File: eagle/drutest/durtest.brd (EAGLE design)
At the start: 100 x 80 mm, 2 parts, among them U1 XC3S400TQ144

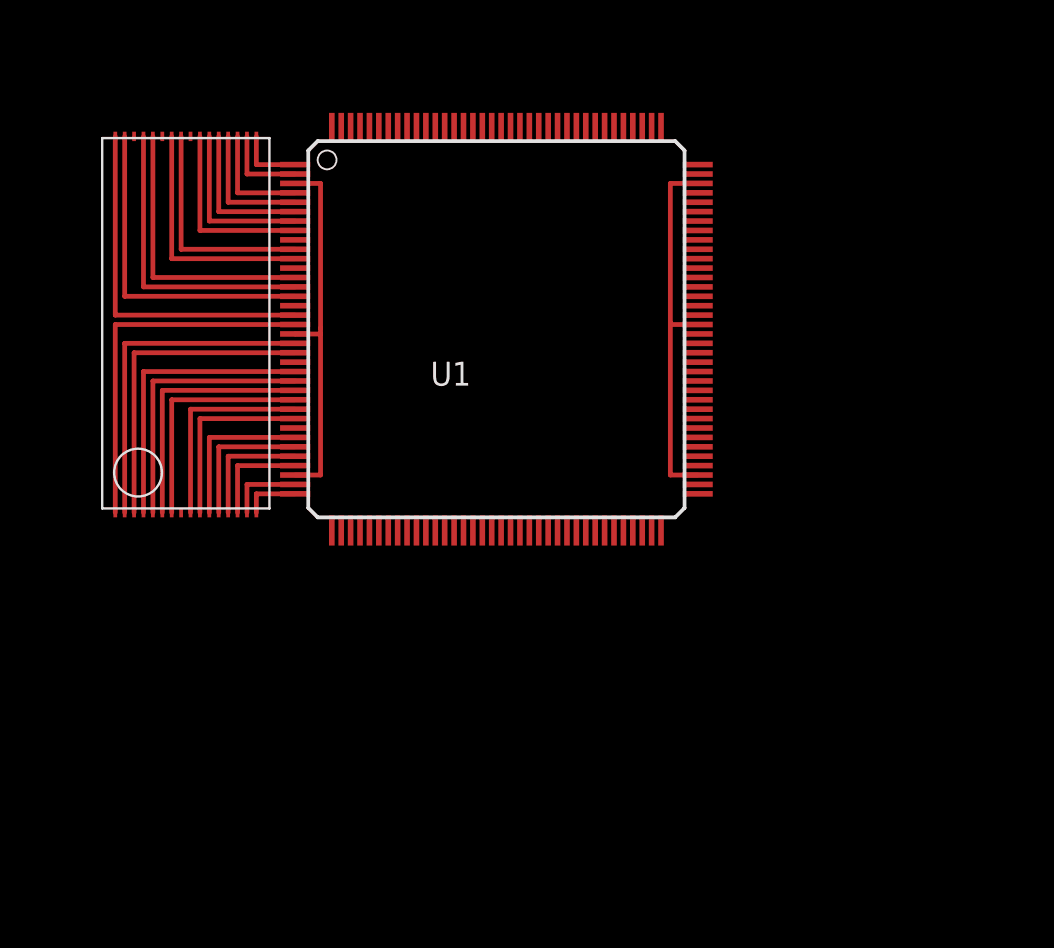
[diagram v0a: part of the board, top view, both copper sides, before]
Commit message: durtest is becoming the best board... but requires proper fabbing
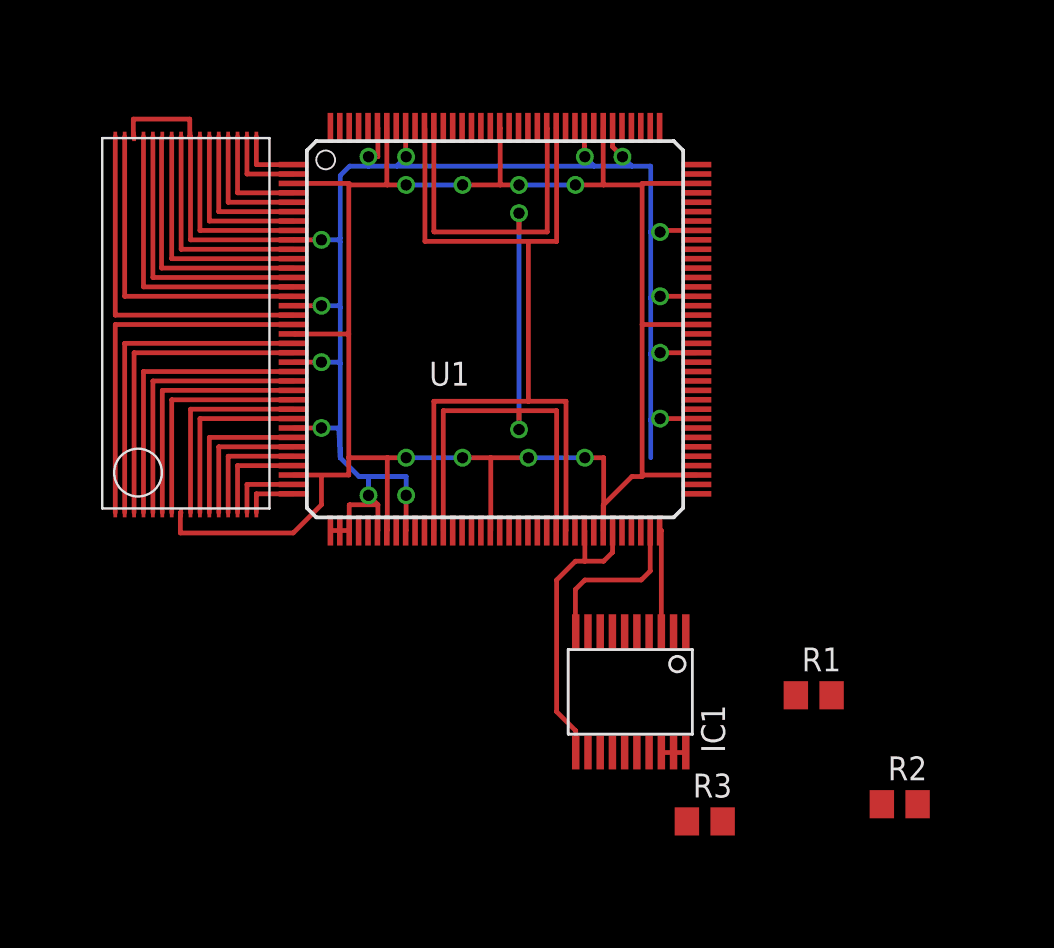
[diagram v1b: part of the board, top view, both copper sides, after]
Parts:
- added IC1: XCF02S, smd-special:VO20
- added R1, R2, R3: 100, rcl:R0805
- moved U1 0.07 mm to (50.7, 36.8)
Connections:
- removed net N$30: U1.P115, U1.P126, U1.P138
- removed net N$31: U1.P106, U1.P75, U1.P91
- removed net N$32: U1.P43, U1.P54, U1.P66
- removed net N$33: U1.P19, U1.P3, U1.P34
- new net GND: IC1.11, U$1.P24, U$1.P30, U1.P101, U1.P114, U1.P117, U1.P136, U1.P139, U1.P16, U1.P22, U1.P29, U1.P37, U1.P38, U1.P39, U1.P42, U1.P45, U1.P64, U1.P67, U1.P81, U1.P88, U1.P9, U1.P94
- new net N$35: IC1.3, U1.P72
- new net N$36: IC1.17, R1.2
- new net N$38: IC1.10, U1.P71
- new net N$39: R2.1, U1.P110
- new net N$40: IC1.7, U1.P143
- new net N$42: R1.1, U1.P144
- new net N$43: R3.1, U1.P111
- new net PROM_DO: IC1.1
- new net PROM_INITB: IC1.8
- new net TCK: IC1.6, R2.2
- new net TDI: IC1.4
- new net TDO: U1.P109
- new net TMS: IC1.5, R3.2
- new net VCC: IC1.18, IC1.19, IC1.20, U$1.P8, U1.P106, U1.P115, U1.P126, U1.P138, U1.P19, U1.P3, U1.P34, U1.P43, U1.P54, U1.P66, U1.P75, U1.P91
- new net VCCAUX: U1.P120, U1.P134, U1.P48, U1.P62
- new net VCCINT: U1.P121, U1.P133, U1.P49, U1.P61
- net N$10: now also U1.P12
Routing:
- net GND: track 0.00 -> 124.2 mm, vias 0 -> 14
- net VCC: track 0.00 -> 114.6 mm, vias 0 -> 8
- net VCCINT: track 0.00 -> 49.4 mm, vias 0 -> 2
- net VCCAUX: track 0.00 -> 48.3 mm
- net N$31: track 19.9 -> 0.00 mm
- net N$33: track 19.6 -> 0.00 mm
- net N$10: track 0.00 -> 13.9 mm
- net N$38: track 0.00 -> 8.76 mm
- net N$35: track 0.00 -> 5.44 mm

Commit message: durtest quite nice
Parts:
- moved R2 12.6 mm to (65.2, 22.1), turned to 270 degrees
- moved R3 11.5 mm to (62.7, 22.1), turned to 270 degrees
- moved R1 4.41 mm to (63.3, 17.1), turned to 180 degrees
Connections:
- net PROM_DO: now also U1.P65
- net PROM_INITB: now also U1.P58
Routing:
- net N$42: track 0.00 -> 56.5 mm, vias 0 -> 2
- net N$40: track 0.00 -> 43.6 mm, vias 0 -> 2
- net N$43: track 0.00 -> 30.4 mm, vias 0 -> 2
- net N$39: track 0.00 -> 29.4 mm, vias 0 -> 2
- net VCC: track 114.6 -> 140.3 mm, vias 8 -> 10
- net GND: track 124.2 -> 144.9 mm, vias 14 -> 15
- net PROM_DO: track 0.00 -> 12.1 mm, vias 0 -> 2
- net TCK: track 0.00 -> 11.9 mm
- net TMS: track 0.00 -> 8.14 mm
- net N$36: track 0.00 -> 8.02 mm
- net PROM_INITB: track 0.00 -> 7.68 mm, vias 0 -> 2
- net VCCINT: track 49.4 -> 50.9 mm
- net VCCAUX: track 48.3 -> 49.8 mm

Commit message: oh, it's really late
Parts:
- added JP1: (no value), pinhead:2X20
- added X1: SCART-F, con-hirschmann:SCART-F
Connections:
- new net N$30: JP1.1, U1.P108
- new net N$31: JP1.39, U1.P73
- new net N$32: JP1.40, U1.P74
- new net N$33: JP1.37, U1.P76
- new net N$34: JP1.38, U1.P77
- new net N$37: JP1.35, U1.P78
- new net N$41: JP1.36, U1.P79
- new net N$44: JP1.33, U1.P80
- new net N$45: JP1.34, U1.P82
- new net N$46: JP1.31, U1.P83
- new net N$47: JP1.32, U1.P84
- new net N$48: JP1.29, U1.P85
- new net N$49: JP1.30, U1.P86
- new net N$50: JP1.27, U1.P87
- new net N$51: JP1.28, U1.P89
- new net N$52: JP1.25, U1.P90
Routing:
- net N$32: track 0.00 -> 34.1 mm
- net N$34: track 0.00 -> 33.1 mm
- net N$41: track 0.00 -> 32.5 mm
- net N$31: track 0.00 -> 31.3 mm
- net N$45: track 0.00 -> 31.1 mm
- net N$33: track 0.00 -> 30.7 mm
- net N$37: track 0.00 -> 29.7 mm
- net N$47: track 0.00 -> 29.2 mm
- net N$44: track 0.00 -> 28.5 mm
- net N$49: track 0.00 -> 27.8 mm
- net N$51: track 0.00 -> 27.0 mm
- net N$46: track 0.00 -> 26.9 mm
- net N$48: track 0.00 -> 25.4 mm
- net N$50: track 0.00 -> 24.2 mm
- net N$52: track 0.00 -> 23.0 mm
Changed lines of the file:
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@@
 <element name="R2" library="rcl" package="R0805" value="100" x="65.2376" y="22.0824" rot="R270"/>
 <element name="R3" library="rcl" package="R0805" value="100" x="62.7244" y="22.118" rot="R270"/>
+<element name="X1" library="con-hirschmann" package="SCART-F" value="SCART-F" x="21.5" y="32.5" rot="R270">
+<attribute name="OC_NEWARK" value="unknown" x="21.5" y="32.5" size="1.778" layer="27" rot="R270" display="off"/>
+<attribute name="MPN" value="" x="21.5" y="32.5" size="1.778" layer="27" rot="R270" display="off"/>
+<attribute name="MF" value="" x="21.5" y="32.5" size="1.778" layer="27" rot="R270" display="off"/>
+<attribute name="OC_FARNELL" value="unknown" x="21.5" y="32.5" size="1.778" layer="27" rot="R270" display="off"/>
+</element>
+<element name="JP1" library="pinhead" package="2X20" value="" x="80" y="34.5" rot="R270"/>
 </elements>
 <signals>
@@
 <wire x1="33" y1="47" x2="33.04" y2="47.08" width="0" layer="19" extent="1-1"/>
 </signal>
+<signal name="N$30">
+<contactref element="U1" pad="P108"/>
+<contactref element="JP1" pad="1"/>
+<wire x1="78.73" y1="58.63" x2="61.425" y2="45.58" width="0" layer="19" extent="1-1"/>
+</signal>
+<signal name="N$31">
+<contactref element="JP1" pad="39"/>
+<contactref element="U1" pad="P73"/>
+<wire x1="78.73" y1="10.37" x2="69.63" y2="10.37" width="0.254" layer="1"/>
+<wire x1="69.63" y1="10.37" x2="66.5" y2="13.5" width="0.254" layer="1"/>
+<wire x1="66.5" y1="13.5" x2="66.5" y2="25" width="0.254" layer="1"/>
+<wire x1="66.5" y1="25" x2="63.5" y2="28" width="0.254" layer="1"/>
+<wire x1="63.5" y1="28" x2="61.5" y2="28" width="0.254" layer="1"/>
+<wire x1="61.5" y1="28" x2="61.425" y2="28.08" width="0" layer="19" extent="1-16"/>
+</signal>
+<signal name="N$32">
+<contactref element="JP1" pad="40"/>
+<contactref element="U1" pad="P74"/>
+<wire x1="61.425" y1="28.58" x2="63.92" y2="28.58" width="0.254" layer="1"/>
+<wire x1="63.92" y1="28.58" x2="67" y2="25.5" width="0.254" layer="1"/>
+<wire x1="67" y1="25.5" x2="67" y2="14" width="0.254" layer="1"/>
+<wire x1="67" y1="14" x2="69.5" y2="11.5" width="0.254" layer="1"/>
+<wire x1="69.5" y1="11.5" x2="80.14" y2="11.5" width="0.254" layer="1"/>
+<wire x1="80.14" y1="11.5" x2="81.27" y2="10.37" width="0.254" layer="1"/>
+</signal>
+<signal name="N$33">
+<contactref element="JP1" pad="37"/>
+<contactref element="U1" pad="P76"/>
+<wire x1="78.73" y1="12.91" x2="69.59" y2="12.91" width="0.254" layer="1"/>
+<wire x1="69.59" y1="12.91" x2="67.5" y2="15" width="0.254" layer="1"/>
+<wire x1="67.5" y1="15" x2="67.5" y2="26" width="0.254" layer="1"/>
+<wire x1="67.5" y1="26" x2="63.92" y2="29.58" width="0.254" layer="1"/>
+<wire x1="61.425" y1="29.58" x2="63.92" y2="29.58" width="0.254" layer="1"/>
+</signal>
+<signal name="N$34">
+<contactref element="JP1" pad="38"/>
+<contactref element="U1" pad="P77"/>
+<wire x1="61.425" y1="30.08" x2="64.42" y2="30.08" width="0.254" layer="1"/>
+<wire x1="64.42" y1="30.08" x2="68" y2="26.5" width="0.254" layer="1"/>
+<wire x1="68" y1="26.5" x2="68" y2="16" width="0.254" layer="1"/>
+<wire x1="68" y1="16" x2="70" y2="14" width="0.254" layer="1"/>
+<wire x1="70" y1="14" x2="80.18" y2="14" width="0.254" layer="1"/>
+<wire x1="80.18" y1="14" x2="81.27" y2="12.91" width="0.254" layer="1"/>
+</signal>
+<signal name="N$37">
+<contactref element="U1" pad="P78"/>
+<contactref element="JP1" pad="35"/>
+<wire x1="78.73" y1="15.45" x2="69.55" y2="15.45" width="0.254" layer="1"/>
+<wire x1="69.55" y1="15.45" x2="68.5" y2="16.5" width="0.254" layer="1"/>
+<wire x1="68.5" y1="16.5" x2="68.5" y2="27" width="0.254" layer="1"/>
+<wire x1="68.5" y1="27" x2="64.92" y2="30.58" width="0.254" layer="1"/>
+<wire x1="61.425" y1="30.58" x2="64.92" y2="30.58" width="0.254" layer="1"/>
+</signal>
+<signal name="N$41">
+<contactref element="JP1" pad="36"/>
+<contactref element="U1" pad="P79"/>
+<wire x1="61.425" y1="31.08" x2="65.42" y2="31.08" width="0.254" layer="1"/>
+<wire x1="65.42" y1="31.08" x2="69" y2="27.5" width="0.254" layer="1"/>
+<wire x1="69" y1="27.5" x2="69" y2="17" width="0.254" layer="1"/>
+<wire x1="69" y1="17" x2="69.5" y2="16.5" width="0.254" layer="1"/>
+<wire x1="69.5" y1="16.5" x2="80.22" y2="16.5" width="0.254" layer="1"/>
+<wire x1="80.22" y1="16.5" x2="81.27" y2="15.45" width="0.254" layer="1"/>
+</signal>
+<signal name="N$44">
+<contactref element="U1" pad="P80"/>
+<contactref element="JP1" pad="33"/>
+<wire x1="61.425" y1="31.58" x2="65.92" y2="31.58" width="0.254" layer="1"/>
+<wire x1="65.92" y1="31.58" x2="69.5" y2="28" width="0.254" layer="1"/>
+<wire x1="69.5" y1="28" x2="69.5" y2="18.5" width="0.254" layer="1"/>
+<wire x1="69.5" y1="18.5" x2="70" y2="18" width="0.254" layer="1"/>
+<wire x1="70" y1="18" x2="78.72" y2="18" width="0.254" layer="1"/>
+<wire x1="78.72" y1="18" x2="78.73" y2="17.99" width="0.254" layer="1"/>
+</signal>
+<signal name="N$45">
+<contactref element="JP1" pad="34"/>
+<contactref element="U1" pad="P82"/>
+<wire x1="61.425" y1="32.58" x2="65.92" y2="32.58" width="0.254" layer="1"/>
+<wire x1="65.92" y1="32.58" x2="70" y2="28.5" width="0.254" layer="1"/>
+<wire x1="70" y1="28.5" x2="70" y2="20" width="0.254" layer="1"/>
+<wire x1="70.5" y1="19.25" x2="70" y2="20" width="0.254" layer="1"/>
+<wire x1="81.5" y1="18" x2="80.26" y2="19.5" width="0" layer="19" extent="1-16"/>
+<wire x1="80.26" y1="19.5" x2="81.27" y2="17.99" width="0" layer="19" extent="1-16"/>
+<wire x1="70.5" y1="19.25" x2="80" y2="19.25" width="0.254" layer="1"/>
+<wire x1="80" y1="19.25" x2="81.5" y2="18" width="0.254" layer="1"/>
+</signal>
+<signal name="N$46">
+<contactref element="U1" pad="P83"/>
+<contactref element="JP1" pad="31"/>
+<wire x1="61.425" y1="33.08" x2="66.42" y2="33.08" width="0.254" layer="1"/>
+<wire x1="66.42" y1="33.08" x2="70.5" y2="29" width="0.254" layer="1"/>
+<wire x1="70.5" y1="29" x2="70.5" y2="21.5" width="0.254" layer="1"/>
+<wire x1="70.5" y1="21.5" x2="71.5" y2="20.5" width="0.254" layer="1"/>
+<wire x1="71.5" y1="20.5" x2="78.7" y2="20.5" width="0.254" layer="1"/>
+<wire x1="78.7" y1="20.5" x2="78.73" y2="20.53" width="0.254" layer="1"/>
+</signal>
+<signal name="N$47">
+<contactref element="JP1" pad="32"/>
+<contactref element="U1" pad="P84"/>
+<wire x1="61.425" y1="33.58" x2="66.92" y2="33.58" width="0.254" layer="1"/>
+<wire x1="66.92" y1="33.58" x2="71" y2="29.5" width="0.254" layer="1"/>
+<wire x1="71" y1="29.5" x2="71" y2="23" width="0.254" layer="1"/>
+<wire x1="71" y1="23" x2="72" y2="22" width="0.254" layer="1"/>
+<wire x1="72" y1="22" x2="80.3" y2="22" width="0.254" layer="1"/>
+<wire x1="80.3" y1="22" x2="81.27" y2="20.53" width="0.254" layer="1"/>
+</signal>
+<signal name="N$48">
+<contactref element="JP1" pad="29"/>
+<contactref element="U1" pad="P85"/>
+<wire x1="61.425" y1="34.08" x2="67.42" y2="34.08" width="0.254" layer="1"/>
+<wire x1="67.42" y1="34.08" x2="71.5" y2="30" width="0.254" layer="1"/>
+<wire x1="71.5" y1="30" x2="71.5" y2="24" width="0.254" layer="1"/>
+<wire x1="71.5" y1="24" x2="72.5" y2="23" width="0.254" layer="1"/>
+<wire x1="72.5" y1="23" x2="78.66" y2="23" width="0.254" layer="1"/>
+<wire x1="78.66" y1="23" x2="78.73" y2="23.07" width="0.254" layer="1"/>
+</signal>
+<signal name="N$49">
+<contactref element="JP1" pad="30"/>
+<contactref element="U1" pad="P86"/>
+<wire x1="61.425" y1="34.58" x2="67.92" y2="34.58" width="0.254" layer="1"/>
+<wire x1="67.92" y1="34.58" x2="72" y2="30.5" width="0.254" layer="1"/>
+<wire x1="72" y1="30.5" x2="72" y2="25" width="0.254" layer="1"/>
+<wire x1="72" y1="25" x2="72.5" y2="24.5" width="0.254" layer="1"/>
+<wire x1="72.5" y1="24.5" x2="79.84" y2="24.5" width="0.254" layer="1"/>
+<wire x1="79.84" y1="24.5" x2="81.27" y2="23.07" width="0.254" layer="1"/>
+</signal>
+<signal name="N$50">
+<contactref element="JP1" pad="27"/>
+<contactref element="U1" pad="P87"/>
+<wire x1="61.425" y1="35.08" x2="68.42" y2="35.08" width="0.254" layer="1"/>
+<wire x1="68.42" y1="35.08" x2="72.5" y2="31" width="0.254" layer="1"/>
+<wire x1="72.5" y1="31" x2="72.5" y2="26" width="0.254" layer="1"/>
+<wire x1="72.5" y1="26" x2="73" y2="25.5" width="0.254" layer="1"/>
+<wire x1="73" y1="25.5" x2="78.62" y2="25.5" width="0.254" layer="1"/>
+<wire x1="78.62" y1="25.5" x2="78.73" y2="25.61" width="0.254" layer="1"/>
+</signal>
+<signal name="N$51">
+<contactref element="JP1" pad="28"/>
+<contactref element="U1" pad="P89"/>
+<wire x1="61.425" y1="36.08" x2="68.42" y2="36.08" width="0.254" layer="1"/>
+<wire x1="68.42" y1="36.08" x2="73" y2="31.5" width="0.254" layer="1"/>
+<wire x1="73" y1="31.5" x2="73" y2="27" width="0.254" layer="1"/>
+<wire x1="73" y1="27" x2="80.38" y2="27" width="0.254" layer="1"/>
+<wire x1="80.38" y1="27" x2="81.27" y2="25.61" width="0.254" layer="1"/>
+</signal>
+<signal name="N$52">
+<contactref element="U1" pad="P90"/>
+<contactref element="JP1" pad="25"/>
+<wire x1="61.425" y1="36.58" x2="68.92" y2="36.58" width="0.254" layer="1"/>
+<wire x1="68.92" y1="36.58" x2="73.5" y2="32" width="0.254" layer="1"/>
+<wire x1="73.5" y1="32" x2="73.5" y2="28.5" width="0.254" layer="1"/>
+<wire x1="73.5" y1="28.5" x2="74" y2="28" width="0.254" layer="1"/>
+<wire x1="74" y1="28" x2="78.58" y2="28" width="0.254" layer="1"/>
+<wire x1="78.58" y1="28" x2="78.73" y2="28.15" width="0.254" layer="1"/>
+</signal>
 </signals>

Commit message: more playing
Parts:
- added C2: 100nF, resistor:C0603
- added C3, C4: (no value), resistor:C0603
- added JP2: (no value), pinhead:2X08
- added Q5, Q6, Q7, Q8: BC848SMD, bc548:SOT23
- added R10, R22, R25, R30: 1000, rcl:R0805
- added R11: 75, rcl:R0805
- added R12: 750, rcl:R0805
- added R13, R16, R27, R32: 680, rcl:R0805
- added R14, R24, R29, R8, R9: 2200, rcl:R0805
- added R15, R26, R31: 270, rcl:R0805
- added R17, R19: 10000, rcl:R0805
- added R18, R20, R28, R33: 4700, rcl:R0805
- added R21: 47000, rcl:R0805
- added R23, R34: (no value), resistor:M0805
- added R4, R5, R6, R7: 10K, rcl:R0805
- added T1, T3: BSS138, zetex:SOT-23
- added T2: BC848, transistor:SOT23
- added U$2: TXO_7C, cpcfpga:OSC_7C
- added X2: SCART-F, con-hirschmann:SCART-F
- added X3: (no value), mini_din:M_DIN6
- X1: value SCART-F -> 1503_04; device con-hirschmann:SCART-F -> con-lumberg:1503_04
- moved X1 42.4 mm to (6.00, -7.00), turned to 0 degrees
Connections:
- new net AINLEFT: X2.6
- new net AINRIGHT: X2.2
- new net AOUTLEFT: JP2.13, R23.1, X2.3
- new net AOUTRIGHT: JP2.15, R34.1, X2.1
- new net AUDLEFT: C3.2
- new net AUDRIGHT: C4.2
- new net B0: R30.1
- new net B1: R29.1
- new net BLUE: JP2.11, X2.7
- new net CASIN: R21.2, T2.2
- new net CLK_5V: R5.1, T1.1, X3.6
- new net COMPIN: X2.20
- new net COMPOUT: JP2.1, X2.19
- new net CSYNC: R8.1
- new net DATA_5V: R7.1, T3.1, X3.1
- new net D_FASTBLANKING: JP2.3, R11.1, R12.2, X2.16
- new net D_MODESWITCH: JP2.9, X2.8
- new net G0: R25.1
- new net G1: R24.1
- new net GREEN: JP2.7, X2.11
- new net N$53: Q6.1, R10.2, R9.2
- new net N$54: Q6.2, R15.2, R16.2, R20.2
- new net N$55: Q8.1, R24.2, R25.2
- new net N$56: Q8.2, R26.2, R27.2, R28.2
- new net N$57: Q7.1, R29.2, R30.2
- new net N$58: Q7.2, R31.2, R32.2, R33.2
- new net N$59: Q5.2, R13.2, R14.2
- new net N$60: C2.2, R18.1, R19.2, T2.1
- new net N$61: C2.1, R17.2, X1.1
- new net N$62: R18.2, R22.2
- new net N$63: Q5.1, R8.2
- new net N$64: C3.1, R23.2
- new net N$65: C4.1, R34.2
- new net N$66: U$2.OUT, U1.P55
- new net PE1: X3.SH1
- new net PE3: X3.SH3
- new net PS2CLK: R4.1, T1.2
- new net PS2DAT: R6.1, T3.2
- new net R0: R10.1
- new net R1: R9.1
- new net RED: JP2.5, X2.15
- new net SCART_BLANKING: JP2.4
- new net SCART_BLUE: JP2.12, R31.1, R32.1, R33.1
- new net SCART_COMP: JP2.2, R13.1, R14.1
- new net SCART_GREEN: JP2.8, R26.1, R27.1, R28.1
- new net SCART_LEFT: JP2.14
- new net SCART_MODE: JP2.10
- new net SCART_RED: JP2.6, R15.1, R16.1, R20.1
- new net SCART_RIGHT: JP2.16
- new net VCC_5V: R5.2, R7.2, X3.5
- new net VCC_B2: R22.1, R4.2, R6.2, T1.3, T2.3, T3.3
- new net VCC_B3: R11.2
- net GND: now also R12.1, R17.1, R19.1, R21.1, U$2.GND, X1.3, X2.13, X2.14, X2.17, X2.18, X2.21, X2.4, X2.5, X2.9, X3.3, X3.SH2
- net VCC: now also Q5.3, Q6.3, Q7.3, Q8.3, U$2.VDD
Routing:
- net GND: track 144.9 -> 240.2 mm
- net AOUTRIGHT: track 0.00 -> 25.0 mm
- net AOUTLEFT: track 0.00 -> 23.7 mm
- net D_MODESWITCH: track 0.00 -> 17.6 mm
- net BLUE: track 0.00 -> 17.2 mm
- net GREEN: track 0.00 -> 15.9 mm
- net N$42: track 56.5 -> 69.1 mm
- net COMPOUT: track 0.00 -> 11.6 mm
- net RED: track 0.00 -> 11.1 mm
- net N$66: track 0.00 -> 7.96 mm
- net D_FASTBLANKING: track 0.00 -> 6.28 mm
- net VCC: track 140.3 -> 145.9 mm, vias 10 -> 8
